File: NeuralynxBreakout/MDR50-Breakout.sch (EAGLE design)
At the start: 3 parts, among them U1 10250-55H3PC

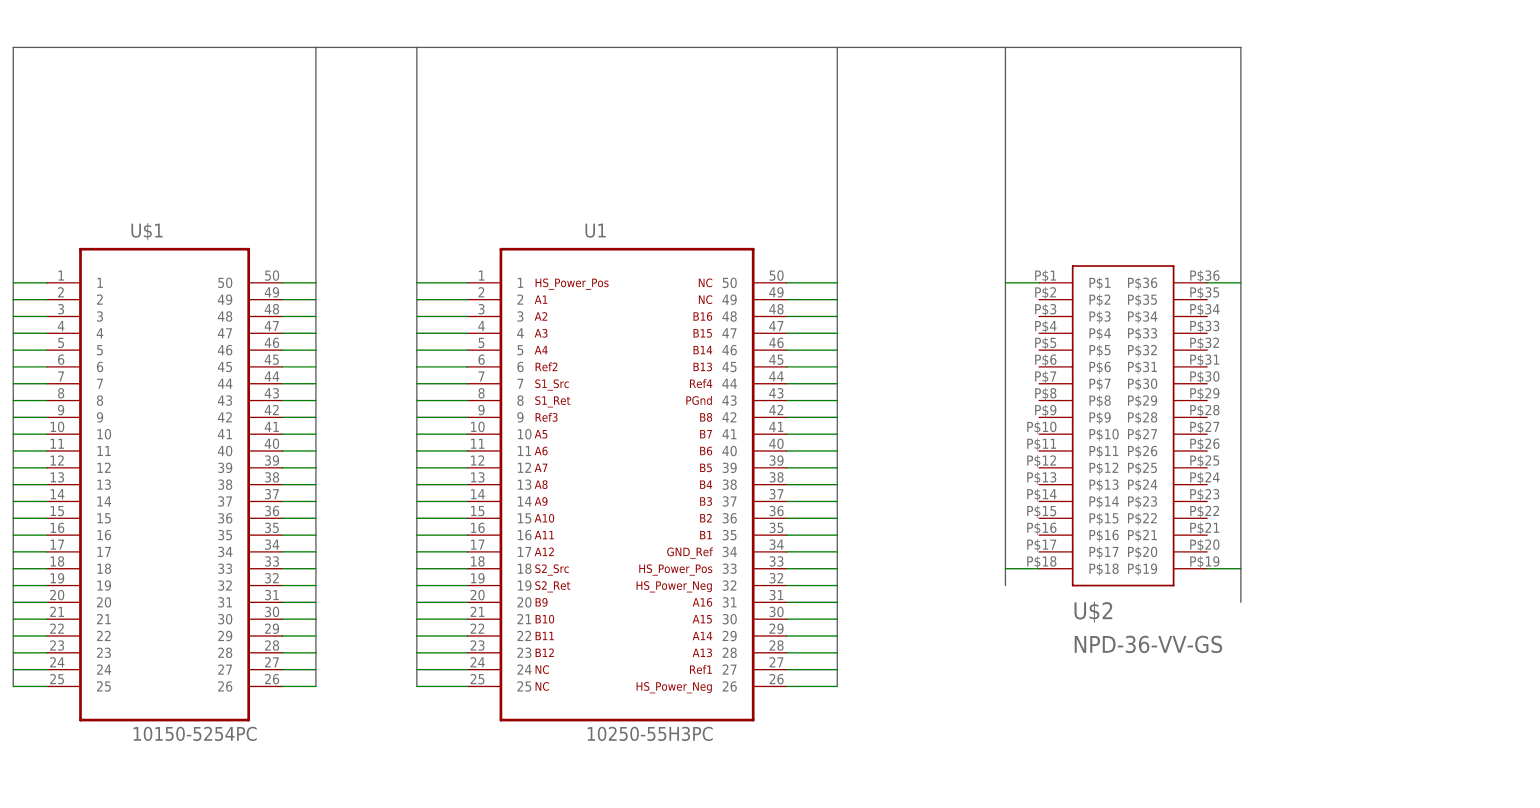
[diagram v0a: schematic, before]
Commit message: Updated, almost finished interface board
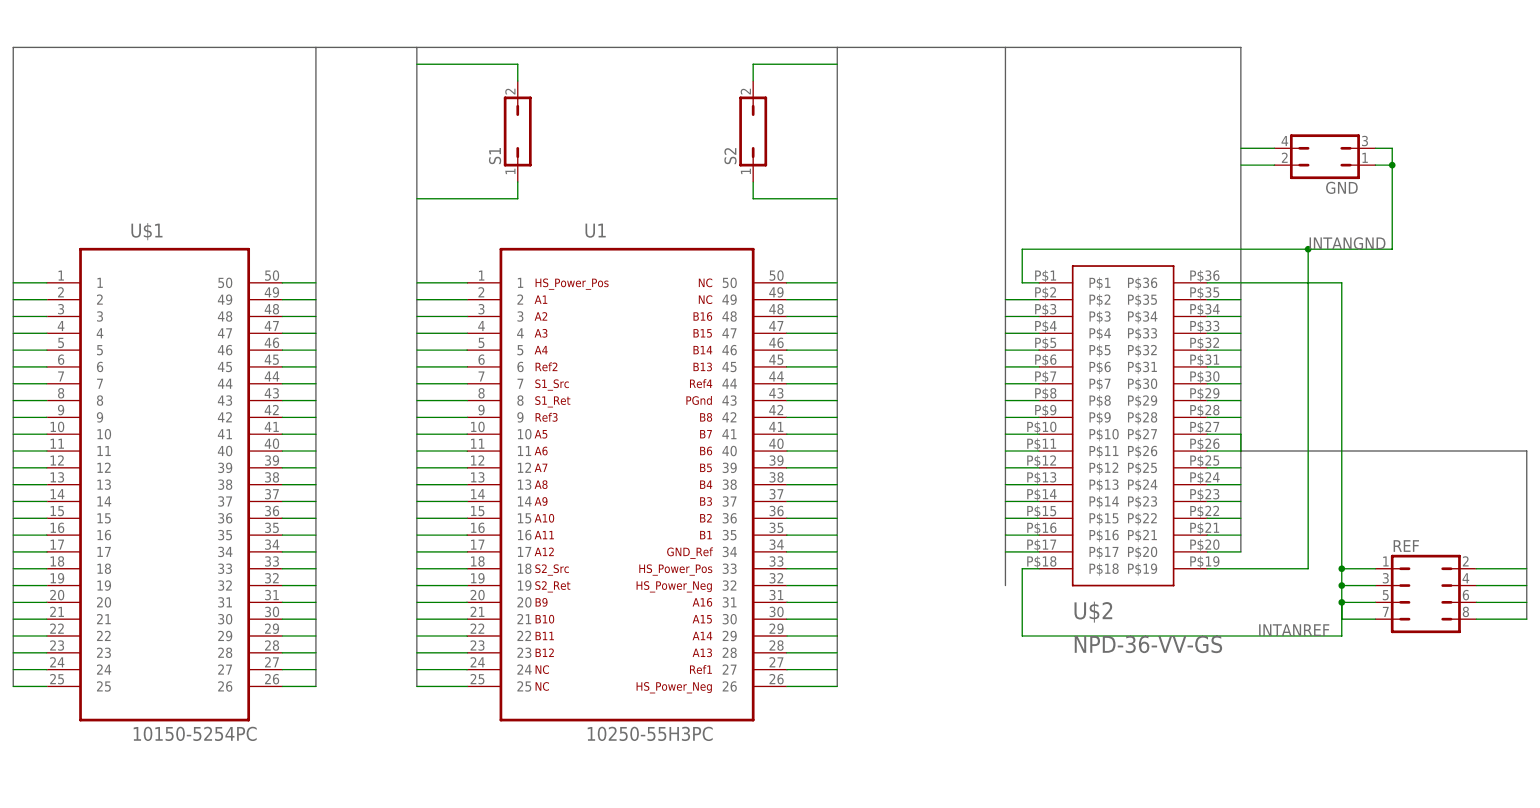
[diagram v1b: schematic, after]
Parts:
- added GND: (no value), jumper:JP2Q
- added REF: (no value), jumper:JP4Q
- added S1, S2: (no value), jumper:JP1Q
- U$1: device Connectors:10150-5254PC -> UsefulConnectors:10150-5254PC
- U1: device Connectors:10250-55H3PC -> UsefulConnectors:10250-55H3PC
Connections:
- new net INTANGND: GND.1, GND.3, U$2.P$1, U$2.P$19
- new net INTANREF: U$2.P$18
- new net N$1: REF.1, REF.3, REF.5, REF.7, U$2.P$36
- net D10: now also U$2.P$14
- net D11: now also U$2.P$15
- net D12: now also U$2.P$16
- net D13: now also U$2.P$17
- net D14: now also U$2.P$20
- net D15: now also U$2.P$21
- net D16: now also U$2.P$22
- net D17: now also U$2.P$23
- net D18: now also S2.1
- net D19: now also S2.2
- net D2: now also U$2.P$10
- net D20: now also U$2.P$2
- net D21: now also U$2.P$3
- net D22: now also U$2.P$4
- net D23: now also U$2.P$5
- net D27: now also REF.2; no longer U$2.P$18, U$2.P$36
- net D28: now also U$2.P$24
- net D29: now also U$2.P$25
- net D3: now also U$2.P$11
- net D30: now also U$2.P$26
- net D31: now also U$2.P$27
- net D34: now also GND.2; no longer U$2.P$1, U$2.P$19
- net D35: now also U$2.P$28
- net D36: now also U$2.P$29
- net D37: now also U$2.P$30
- net D38: now also U$2.P$31
- net D39: now also U$2.P$32
- net D4: now also U$2.P$12
- net D40: now also U$2.P$33
- net D41: now also U$2.P$34
- net D42: now also U$2.P$35
- net D43: now also GND.4
- net D44: now also REF.8
- net D45: now also U$2.P$6
- net D46: now also U$2.P$7
- net D47: now also U$2.P$8
- net D48: now also U$2.P$9
- net D5: now also U$2.P$13
- net D6: now also REF.4
- net D7: now also S1.1
- net D8: now also S1.2
- net D9: now also REF.6

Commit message: Updated Neuralynx breakout board before manufacturing
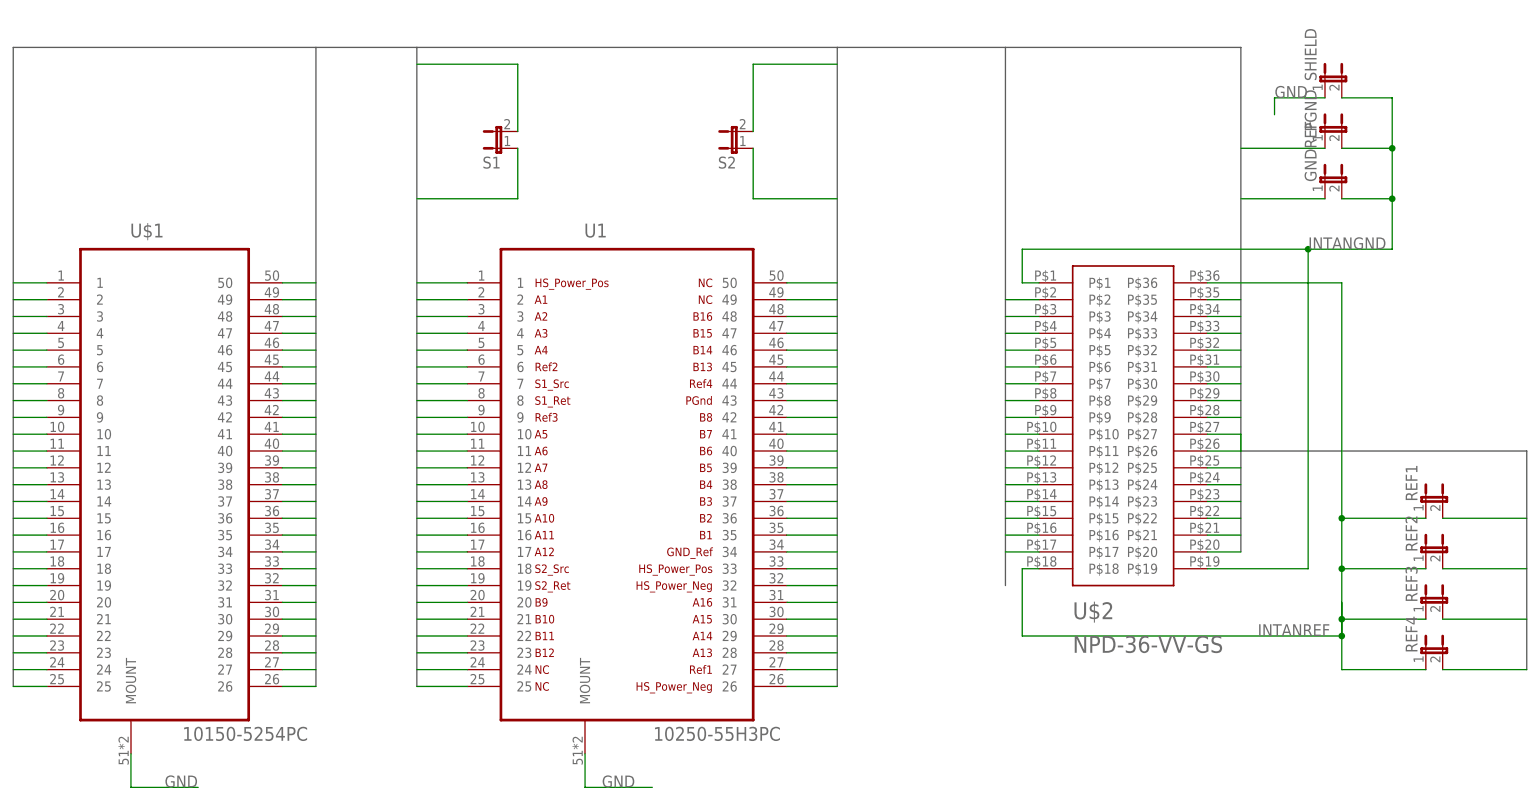
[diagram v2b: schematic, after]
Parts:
- removed GND: (no value), jumper:JP2Q
- removed REF: (no value), jumper:JP4Q
- added GNDREF, PGND, REF1, REF2, REF3, REF4, SHIELD: (no value), SparkFun:JUMPER-2PTH
- S1, S2: device jumper:JP1Q -> SparkFun:JUMPER-2PTH
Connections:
- removed net N$1: REF.1, REF.3, REF.5, REF.7, U$2.P$36
- new net GND: SHIELD.1, U$1.MOUNT, U1.MOUNT
- net D27: now also REF1.2; no longer REF.2
- net D34: now also GNDREF.1; no longer GND.2
- net D43: now also PGND.1; no longer GND.4
- net D44: now also REF4.2; no longer REF.8
- net D6: now also REF2.2; no longer REF.4
- net D9: now also REF3.2; no longer REF.6
- net INTANGND: now also GNDREF.2, PGND.2, SHIELD.2; no longer GND.1, GND.3
- net INTANREF: now also REF1.1, REF2.1, REF3.1, REF4.1, U$2.P$36
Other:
- moved on the sheet: S1, S2
